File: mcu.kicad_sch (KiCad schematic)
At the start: 8 parts, among them J20 LOLIN-S3 (L), J21 LOLIN-S3 (R), J22 ESP32-S3-DEVKITC-1 (L), J23 ESP32-S3-DEVKITC-1 (R), J24 LOLIN-S3-MINI (L), J25 LOLIN-S3-MINI (R), J26 LOLIN-S2-MINI (L), J27 LOLIN-S2-MINI (R)

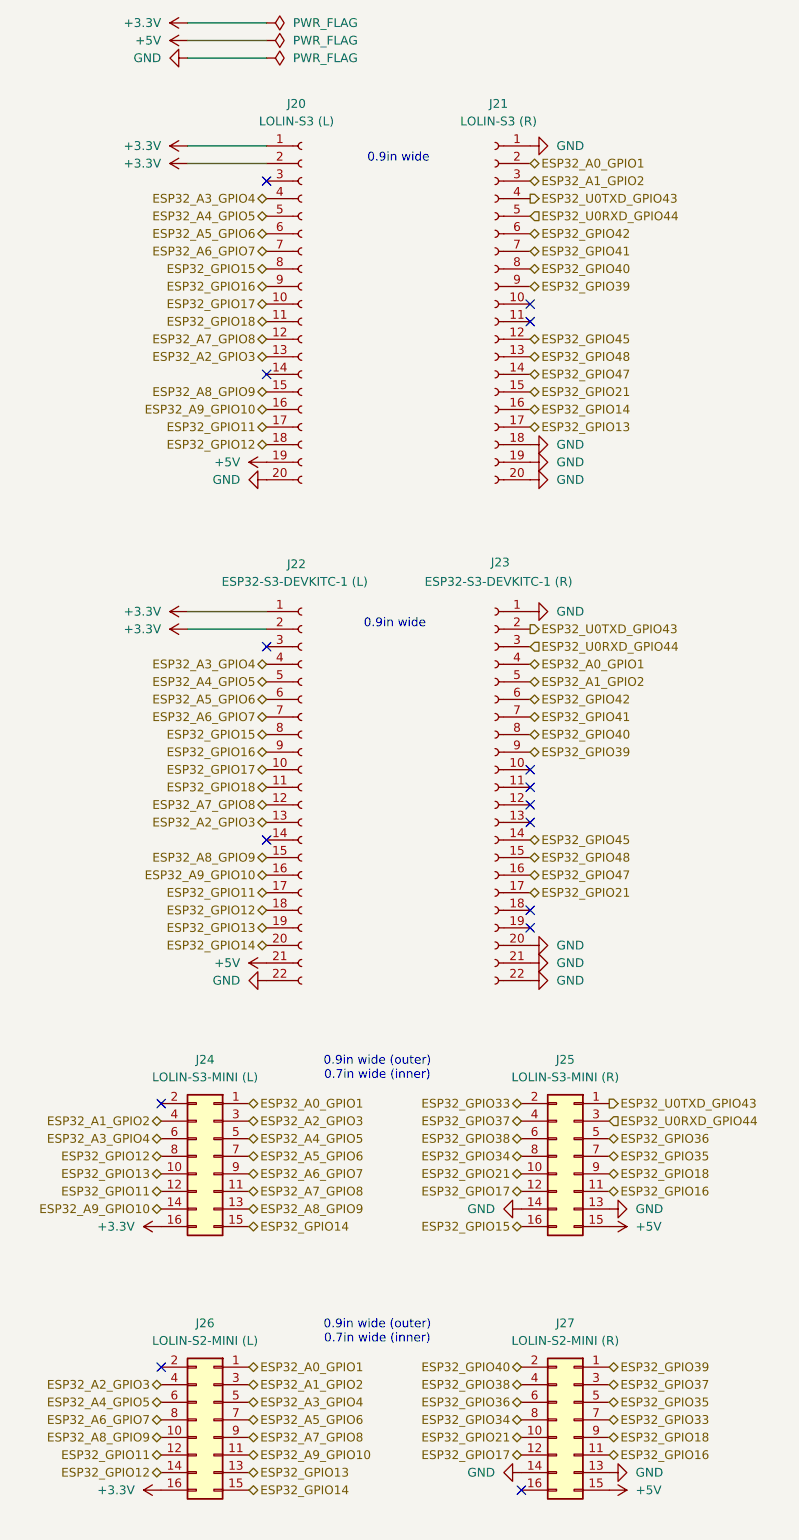
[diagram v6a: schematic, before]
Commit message: Don't connect unused GPIOs together across MCUs
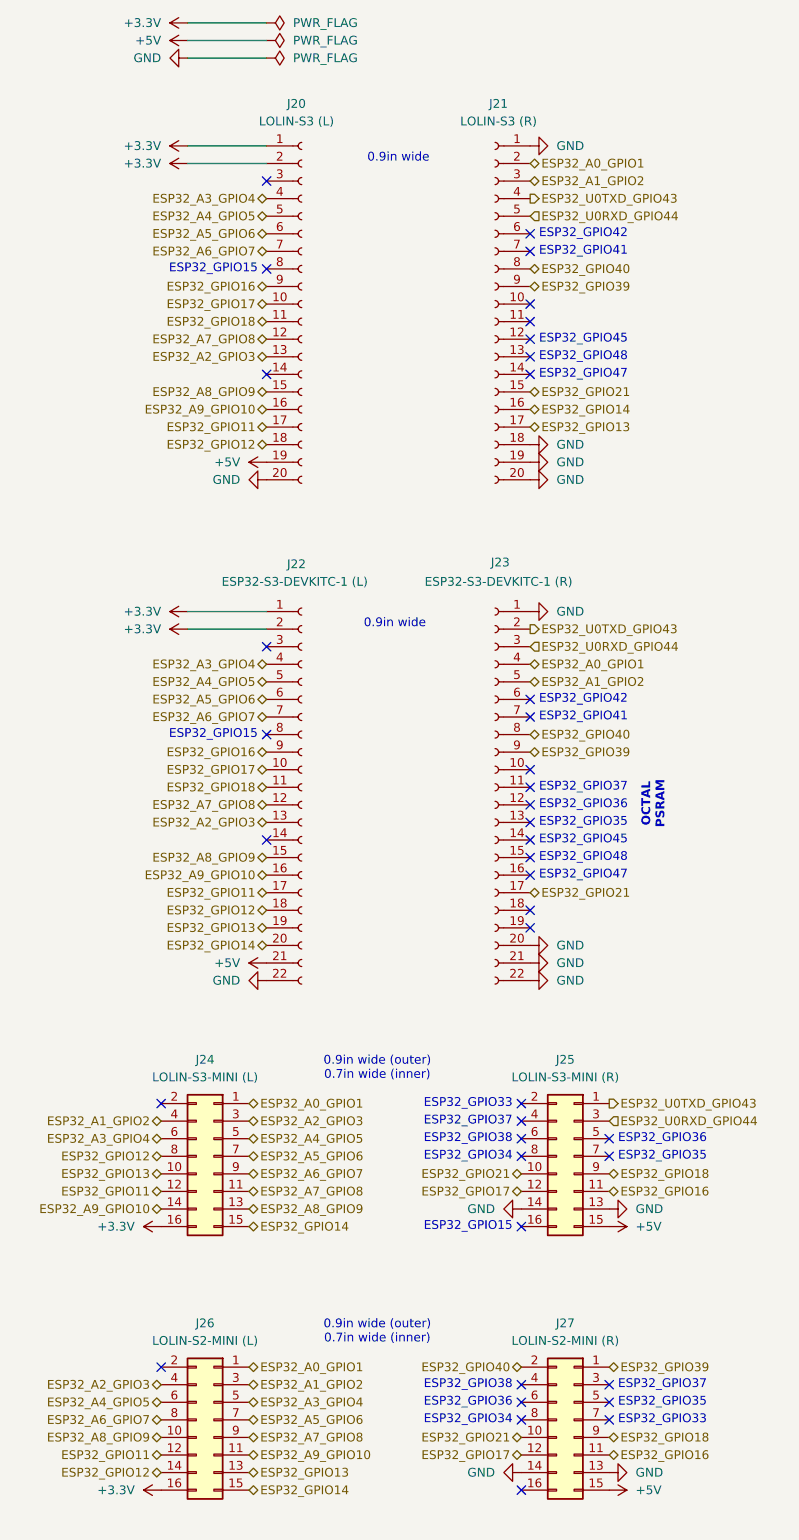
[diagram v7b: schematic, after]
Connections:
- removed net ESP32_GPIO15: J20.8 (Pin_8), J22.8 (Pin_8), J25.16 (Pin_16)
- net ESP32_GPIO33: no longer names the net of J25.2 (Pin_2)
- net ESP32_GPIO33: no longer J27.7 (Pin_7)
- net ESP32_GPIO34: no longer names the net of J25.8 (Pin_8)
- net ESP32_GPIO34: no longer J27.8 (Pin_8)
- net ESP32_GPIO35: no longer names the net of J25.7 (Pin_7)
- net ESP32_GPIO35: no longer J27.5 (Pin_5)
- net ESP32_GPIO36: no longer names the net of J25.5 (Pin_5)
- net ESP32_GPIO36: no longer J27.6 (Pin_6)
- net ESP32_GPIO37: no longer names the net of J25.4 (Pin_4)
- net ESP32_GPIO37: no longer J27.3 (Pin_3)
- net ESP32_GPIO38: no longer names the net of J25.6 (Pin_6)
- net ESP32_GPIO38: no longer J27.4 (Pin_4)
- net ESP32_GPIO41: no longer names the net of J21.7 (Pin_7)
- net ESP32_GPIO41: no longer J23.7 (Pin_7)
- net ESP32_GPIO42: no longer names the net of J21.6 (Pin_6)
- net ESP32_GPIO42: no longer J23.6 (Pin_6)
- net ESP32_GPIO45: no longer names the net of J21.12 (Pin_12)
- net ESP32_GPIO45: no longer J23.14 (Pin_14)
- net ESP32_GPIO47: no longer names the net of J21.14 (Pin_14)
- net ESP32_GPIO47: no longer J23.16 (Pin_16)
- net ESP32_GPIO48: no longer names the net of J21.13 (Pin_13)
- net ESP32_GPIO48: no longer J23.15 (Pin_15)
- no-connect marks 15 -> 40
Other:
- note added: "ESP32_GPIO15"
- note added: "ESP32_GPIO33"
- note added: "ESP32_GPIO34"
- note added: "ESP32_GPIO35"
- note added: "ESP32_GPIO36"
- note added: "ESP32_GPIO37"
- note added: "ESP32_GPIO38"
- note added: "ESP32_GPIO41"
- note added: "ESP32_GPIO42"
- note added: "ESP32_GPIO45"
- note added: "ESP32_GPIO47"
- note added: "ESP32_GPIO48"
- note added: "OCTAL PSRAM"

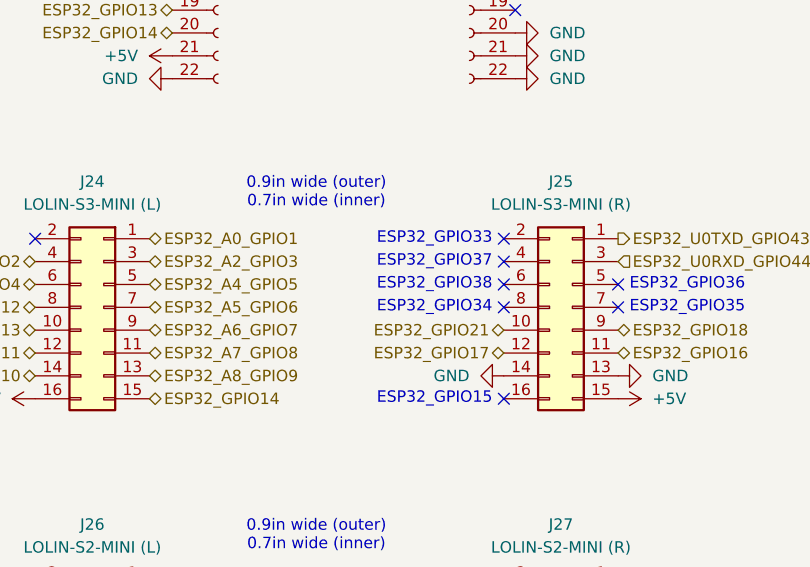
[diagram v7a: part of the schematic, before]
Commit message: First routing attempt
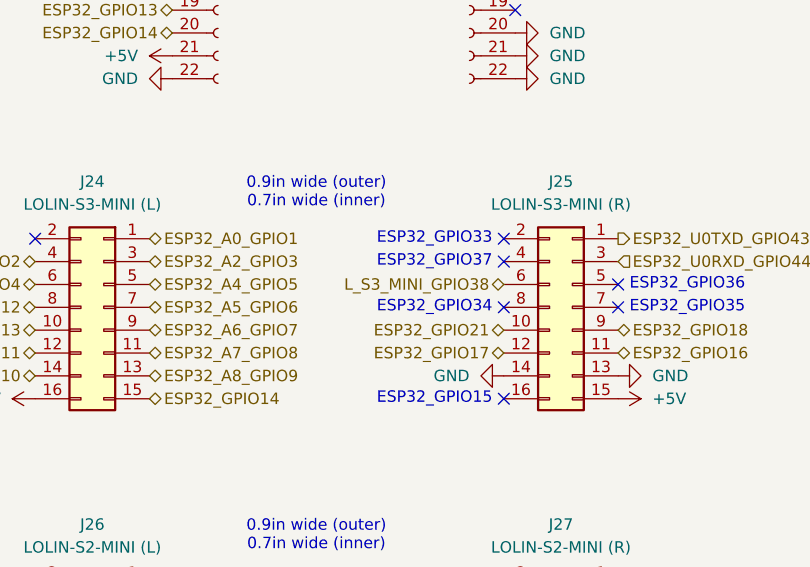
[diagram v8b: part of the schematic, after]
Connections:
- net L_S3_MINI_GPIO38: now reaches J25.6 (Pin_6)
- no-connect marks 40 -> 39
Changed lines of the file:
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@@
-	(text "ESP32_GPIO38"
-		(exclude_from_sim no)
-		(at 71.12 167.64 0)
-		(effects
-			(font
-				(size 1.27 1.27)
-			)
-			(justify right)
-		)
-	)
 	(text "ESP32_GPIO38"
 		(exclude_from_sim no)
@@
 	)
 	(no_connect
-		(at 72.39 167.64)
-	)
-	(no_connect
 		(at 73.66 137.16)
 	)
@@
 		)
 	)
+	(hierarchical_label "L_S3_MINI_GPIO38"
+		(shape bidirectional)
+		(at 72.39 167.64 180)
+		(effects
+			(font
+				(size 1.27 1.27)
+			)
+			(justify right)
+		)
+	)
